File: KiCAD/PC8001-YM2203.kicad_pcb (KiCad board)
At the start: 2 copper layers, 100 x 75 mm, 32 parts, among them J1 PC-8001 ext BUS, J2 ADDR JP, J3 Audio-Jack-3_2Switches, J4 A-CON, J5 B-CON, U1 NJM5532DD, U2 74LS32, U3 74LS138, U4 DLO555MB, U5 YM2203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

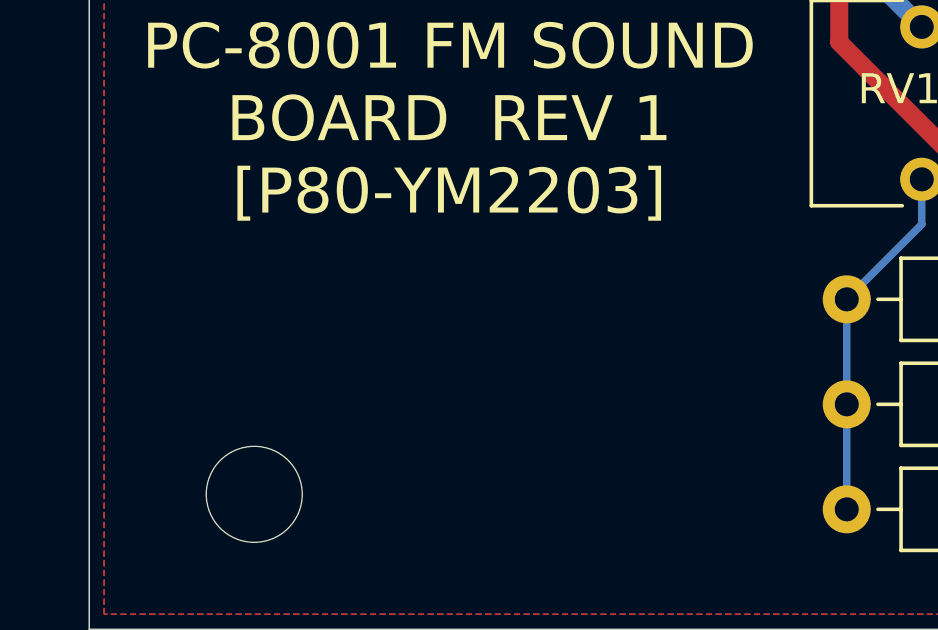
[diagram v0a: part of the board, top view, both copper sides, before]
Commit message: シルク見直し・ガーバー再出力
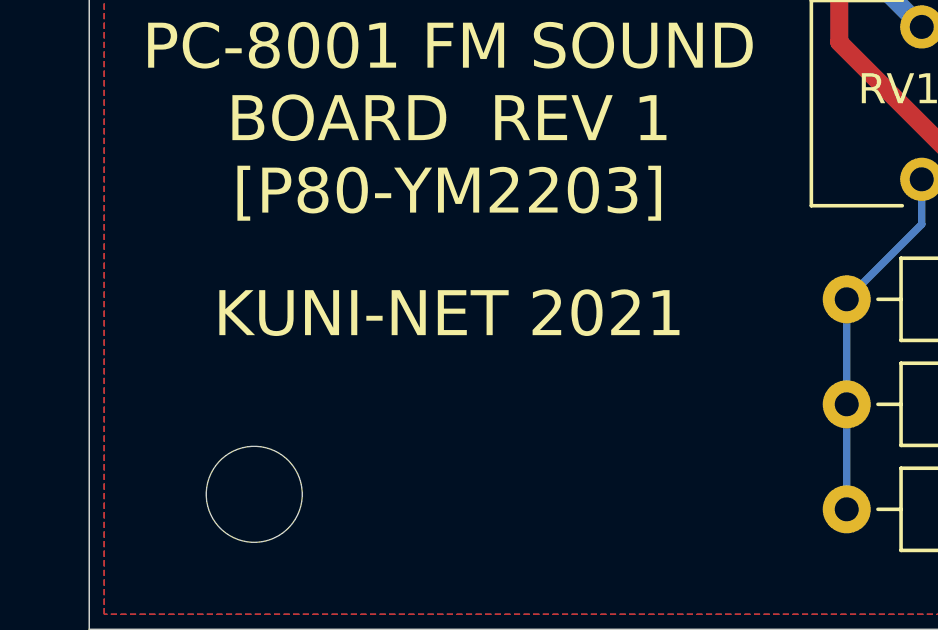
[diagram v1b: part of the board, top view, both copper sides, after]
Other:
- board text added: "KUNI-NET 2021"
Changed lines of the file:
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@@
   (general
     (thickness 1.6)
-    (drawings 22)
+    (drawings 23)
     (tracks 599)
     (zones 0)
@@
     )
   )
+  (gr_text "KUNI-NET 2021" (at 54 125.5) (layer F.SilkS)
+    (effects (font (size 1.5 1.5) (thickness 0.2)))
+  )
   (gr_text 3.579545MHz (at 132.5 79 90) (layer F.SilkS)

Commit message: シルク再見直し・ガーバー再出力
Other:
- board text added: "PC-8001 FM SOUND BOARD REV 1 [KP80-YM2203]"
- board text removed: "PC-8001 FM SOUND BOARD REV 1 [P80-YM2203]"
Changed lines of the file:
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@@
     )
   )
-  (gr_text "KUNI-NET 2021" (at 54 125.5) (layer F.SilkS)
-    (effects (font (size 1.5 1.5) (thickness 0.2)))
+  (gr_text "KUNI-NET 2021" (at 56.5 124.5) (layer F.SilkS)
+    (effects (font (size 1 1) (thickness 0.2)))
   )
   (gr_text 3.579545MHz (at 132.5 79 90) (layer F.SilkS)
@@
     (effects (font (size 1 1) (thickness 0.15)))
   )
-  (gr_text "PC-8001 FM SOUND\nBOARD  REV 1\n[P80-YM2203]" (at 54 119) (layer F.SilkS)
+  (gr_text "PC-8001 FM SOUND\nBOARD  REV 1\n[KP80-YM2203]" (at 54 119) (layer F.SilkS)
     (effects (font (size 1.5 1.5) (thickness 0.2)))
   )
